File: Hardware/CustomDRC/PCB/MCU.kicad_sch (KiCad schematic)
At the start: 6 parts, among them J401 TC2030NL - For UART PROG, U401 ESP32-WROOM-32UE-R2

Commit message: Update - finished schematic for revision A
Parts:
- added D401: LED_Small, LED_SMD:LED_0603_1608Metric_Pad1.05x0.95mm_HandSolder, symbol Device:LED_Small
- added R402, R403: 330R, Resistor_SMD:R_0603_1608Metric_Pad0.98x0.95mm_HandSolder, symbol Device:R_Small
- added TP304, TP306, TP401: TestPoint_Small, TestPoint:TestPoint_Pad_D1.5mm, symbol Connector:TestPoint_Small
- C401: value C_Small -> 1u; footprint (none) -> Capacitor_SMD:C_0603_1608Metric_Pad1.08x0.95mm_HandSolder; LCSC (none) -> C15849; MPN (none) -> CL10A105KB8NNNC; Manufacturer (none) -> Samsung Electro-Mechanics
- C402: footprint (none) -> Capacitor_SMD:C_0805_2012Metric_Pad1.18x1.45mm_HandSolder; LCSC (none) -> C45783; MPN (none) -> CL21A226MAQNNNE; Manufacturer (none) -> Samsung Electro-Mechanics
- C403: footprint (none) -> Capacitor_SMD:C_0603_1608Metric_Pad1.08x0.95mm_HandSolder; LCSC (none) -> C15849; MPN (none) -> CL10A105KB8NNNC; Manufacturer (none) -> Samsung Electro-Mechanics
- R401: value R_Small -> 10k; footprint (none) -> Resistor_SMD:R_0603_1608Metric_Pad0.98x0.95mm_HandSolder; LCSC (none) -> C25804; MPN (none) -> 0603WAF1002T5E; Manufacturer (none) -> UNI-ROYAL(Uniroyal Elec)
- U401: LCSC (none) -> C701346; MPN (none) -> ESP32-WROOM-32UE-N16; Manufacturer (none) -> Espressif Systems
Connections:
- net GND: now also D401.1 (K)
- net IO25: now reaches U401.10 (IO25)
- net IO25: now also R402.1
- net at U401.11 (IO26): now also TP304.1
- net at U401.12 (IO27): now also TP306.1
- net at U401.16 (IO13): now also TP401.1
- net DSP_EN: now reaches U401.29 (IO5)
- net DSP_EN: now also R403.1
- net IO18: now reaches U401.30 (IO18)
- net IO19: now reaches U401.31 (IO19)
- net IO21: now reaches U401.33 (IO21)
- net GPIO36: now reaches U401.4 (SENSOR_VP)
- net GPIO39: now reaches U401.5 (SENSOR_VN)
- net IO34: now reaches U401.6 (IO34)
- net IO35: now reaches U401.7 (IO35)
- net IO32: now reaches U401.8 (IO32)
- net IO33: now reaches U401.9 (IO33)
- new net: D401.2 (A), R402.2
- new net IO5: R403.2
- no-connect marks 2 -> 8
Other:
- note added: "MCU: ESP32-WROOM-32UE-R2"
- note added: "STRAPPING PINS: GPIO0: BOOT MODE GPIO2: MUST BE FLOATING OR LOW TO ENTER FLASHING MODE GPIO6-GPIO11 - INTEGRATED FLASH SPI PINS GPIO12: FAILS TO BOOT IF PULLED HIGH GPIO14: OUTPUTS PWM ON BOOT GPIO15: OUTPUTS PWM ON BOOT & STRAPPING"
- company: (none) -> JS HW
- title: (none) -> CDRC - Custom DRC for Audison AC Link
- moved on the sheet: C401, C402, C403, J401, R401, U401

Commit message: Sync HW changes for V1 PCB
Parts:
- D401: value LED_Small -> WHITE OR BLUE; MPN KT-0603W -> KT-0603W
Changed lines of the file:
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@@
 	(title_block
 		(title "CDRC - Custom DRC for Audison AC Link")
-		(date "2024-08-20")
+		(date "03-09-2024")
 		(rev "A")
 		(company "JS HW")
@@
 			)
 		)
-		(property "Value" "LED_Small"
+		(property "Value" "WHITE OR BLUE"
 			(at 170.18 134.5564 90)
 			(effects
@@
 			)
 		)
-		(property "MPN" " KT-0603W"
+		(property "MPN" "KT-0603W"
 			(at 167.64 133.35 0)
 			(effects

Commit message: Sync before making breaking changes to RS485 comms protocl and method
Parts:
- removed TP401: TestPoint_Small, TestPoint:TestPoint_Pad_D1.5mm, symbol Connector:TestPoint_Small
- added TP305, TP307, TP308: TestPoint_Small, TestPoint:TestPoint_Pad_D1.5mm, symbol Connector:TestPoint_Small
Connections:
- net IO21 is gone; now on an unnamed net: U401.33 (IO21)
- net at TP306.1: no longer U401.12 (IO27)
- net at U401.16 (IO13): now also TP308.1
- net at U401.26 (IO4): now also TP307.1
- net at U401.28 (IO17): now also TP305.1
- net GPIO36 renamed IO36
- net GPIO39 renamed IO39
- new net IO27: U401.12 (IO27)
- no-connect marks 8 -> 6
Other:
- title: CDRC - Custom DRC for Audison AC Link -> CDRC - Custom DRC for Bit 10D
- moved on the sheet: TP304, TP306

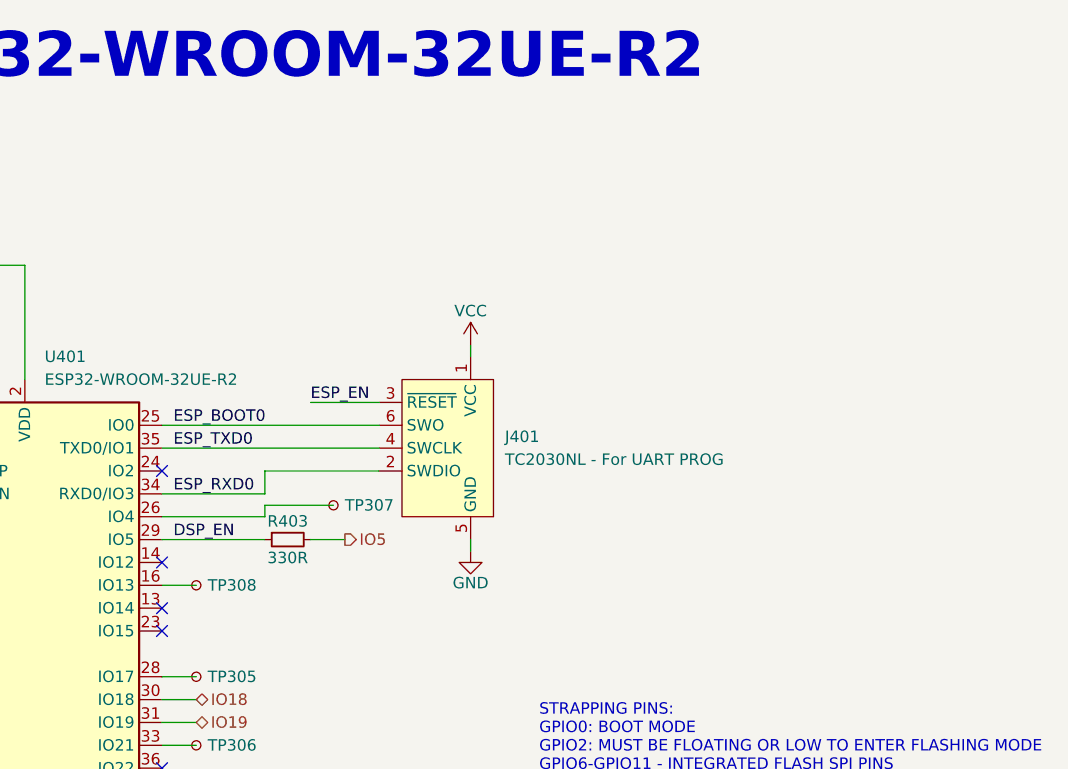
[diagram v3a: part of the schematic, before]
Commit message: Added board renders and PDF plots
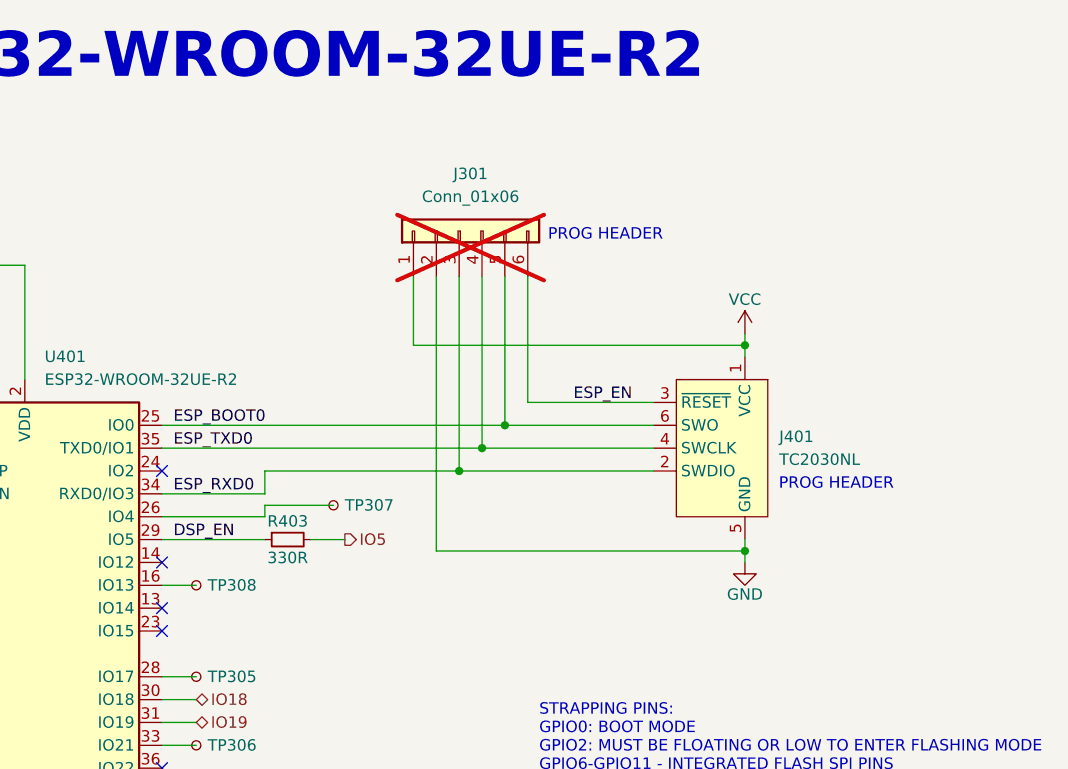
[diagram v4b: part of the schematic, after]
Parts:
- added J301: Conn_01x06, Connector_PinSocket_2.54mm:PinSocket_1x06_P2.54mm_Vertical, symbol Connector_Generic:Conn_01x06
- D401: LCSC C2290 -> C2290
- J401: value TC2030NL - For UART PROG -> TC2030NL
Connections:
- net ESP_BOOT0: now also J301.5 (Pin_5)
- net ESP_EN: now also J301.6 (Pin_6)
- net ESP_RXD0: now also J301.3 (Pin_3)
- net ESP_TXD0: now also J301.4 (Pin_4)
- net GND: now also J301.2 (Pin_2)
- net VCC: now also J301.1 (Pin_1)
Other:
- note added: "PROG HEADER"
- moved on the sheet: J401
